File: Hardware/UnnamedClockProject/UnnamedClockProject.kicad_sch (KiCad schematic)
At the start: 28 parts, among them J101 CLOCK_OUT, J102 POWER, Q101 2N3904, U104 G3MB-202P, U105 G3MB-202P, U106 G3MB-202P, U107 CAT24C256

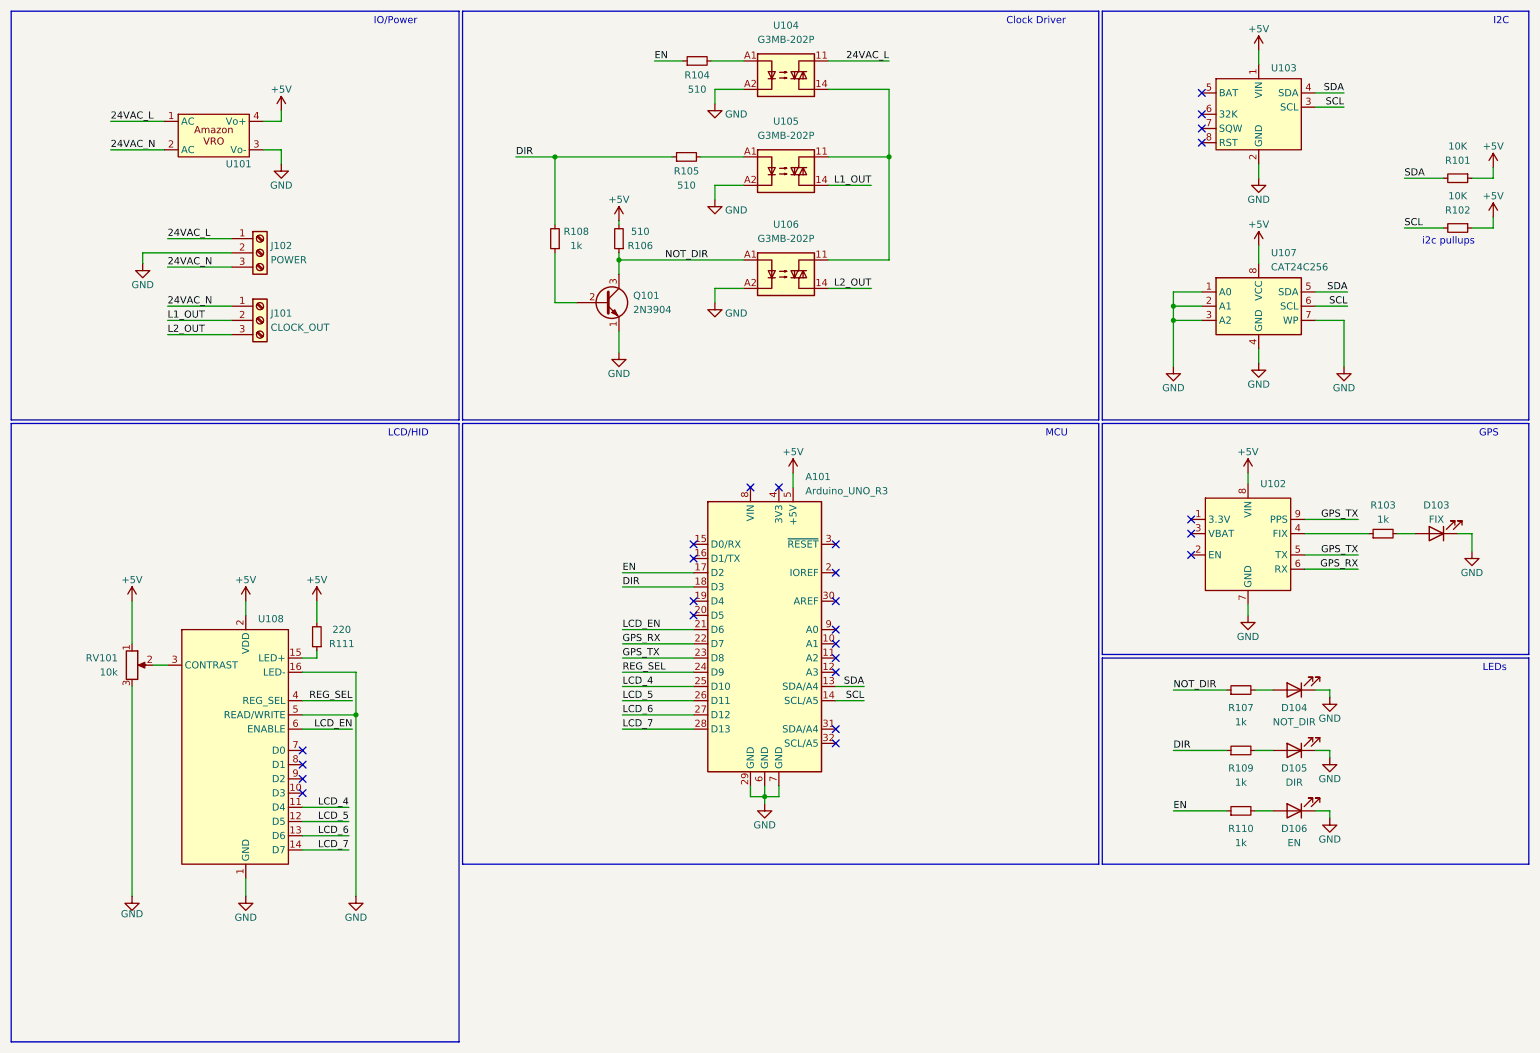
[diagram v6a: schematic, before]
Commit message: fix ERC
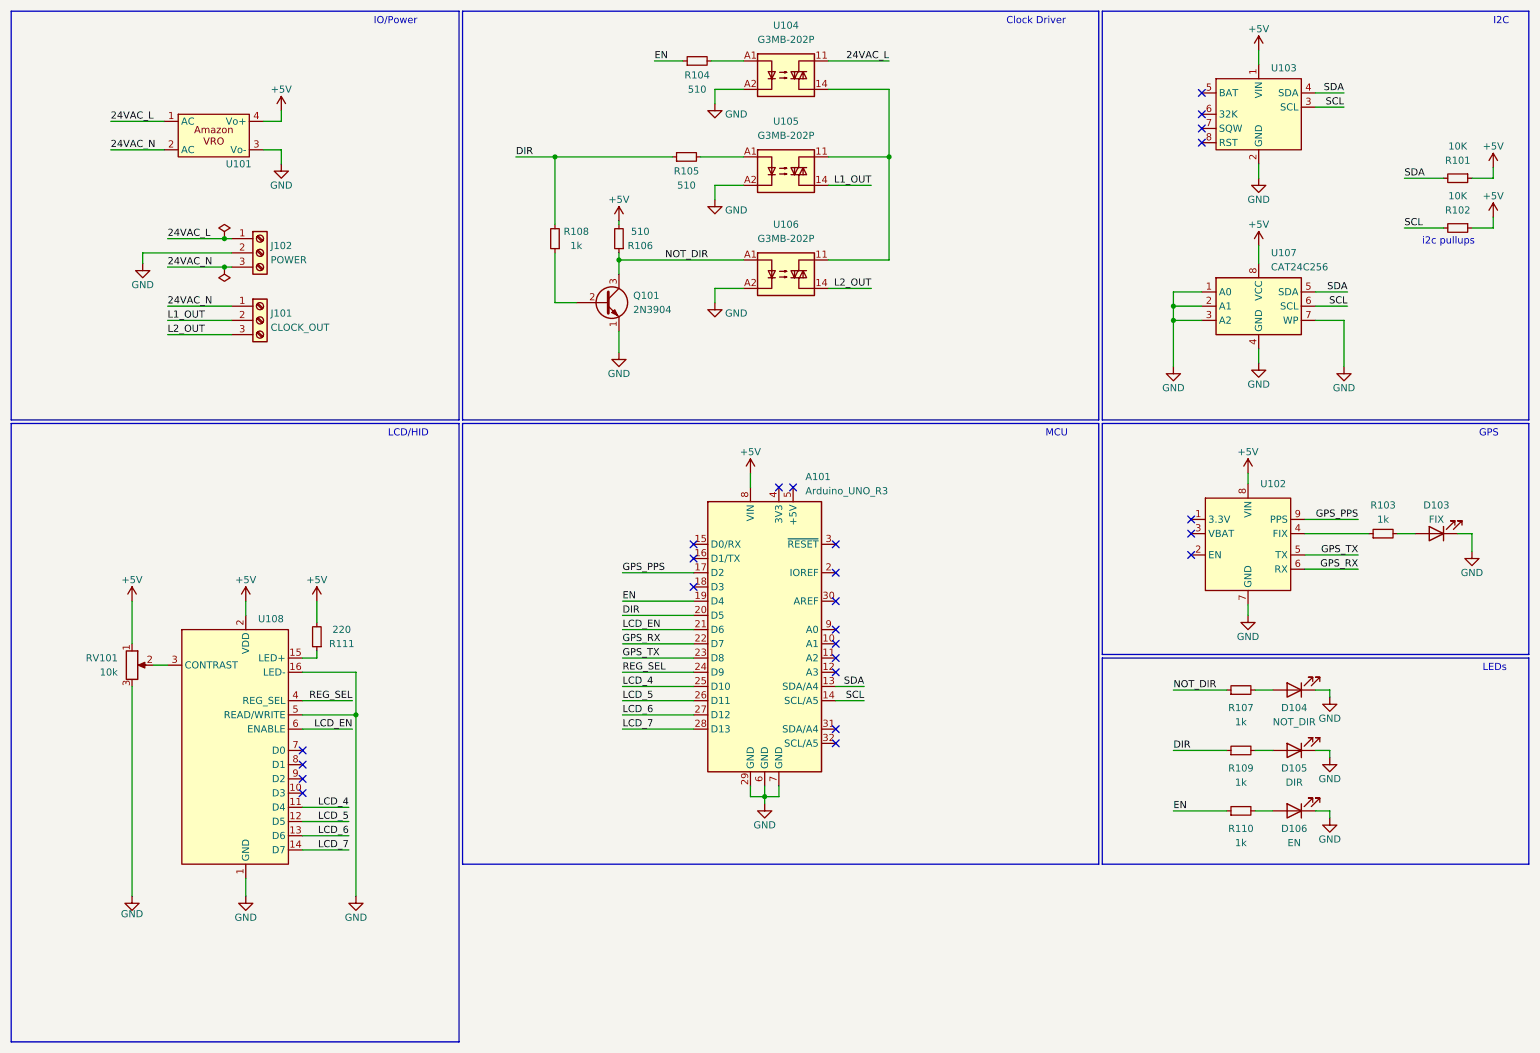
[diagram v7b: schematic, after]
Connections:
- net +5V: now also A101.8 (VIN); no longer A101.5 (+5V)
- net DIR: now also A101.20 (D5); no longer A101.18 (D3)
- net EN: now also A101.19 (D4); no longer A101.17 (D2)
- net GPS_TX: no longer U102.9 (PPS)
- new net GPS_PPS: A101.17 (D2), U102.9 (PPS)
- no-connect marks 26 -> 25

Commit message: bump
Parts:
- R101, R102, R103, R104, R105, R106, R107, R108, R109, R110, R111: footprint (none) -> Resistor_THT:R_Axial_DIN0207_L6.3mm_D2.5mm_P10.16mm_Horizontal
- RV101: footprint (none) -> Potentiometer_THT:Potentiometer_Bourns_3339S_Horizontal
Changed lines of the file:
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@@
       (effects (font (size 1.27 1.27)) (justify right))
     )
-    (property "Footprint" "" (at 34.925 129.54 0)
+    (property "Footprint" "Potentiometer_THT:Potentiometer_Bourns_3339S_Horizontal" (at 34.925 129.54 0)
       (effects (font (size 1.27 1.27)) hide)
     )
@@
       (effects (font (size 1.27 1.27)))
     )
-    (property "Footprint" "" (at 67.945 124.46 0)
+    (property "Footprint" "Resistor_THT:R_Axial_DIN0207_L6.3mm_D2.5mm_P10.16mm_Horizontal" (at 67.945 124.46 0)
       (effects (font (size 1.27 1.27)) hide)
     )
@@
       (effects (font (size 1.27 1.27)))
     )
-    (property "Footprint" "" (at 121.92 53.34 0)
+    (property "Footprint" "Resistor_THT:R_Axial_DIN0207_L6.3mm_D2.5mm_P10.16mm_Horizontal" (at 121.92 53.34 0)
       (effects (font (size 1.27 1.27)) hide)
     )
@@
       (effects (font (size 1.27 1.27)))
     )
-    (property "Footprint" "" (at 135.89 21.59 0)
+    (property "Footprint" "Resistor_THT:R_Axial_DIN0207_L6.3mm_D2.5mm_P10.16mm_Horizontal" (at 135.89 21.59 0)
       (effects (font (size 1.27 1.27)) hide)
     )
@@
       (effects (font (size 1.27 1.27)))
     )
-    (property "Footprint" "" (at 233.045 155.575 0)
+    (property "Footprint" "Resistor_THT:R_Axial_DIN0207_L6.3mm_D2.5mm_P10.16mm_Horizontal" (at 233.045 155.575 0)
       (effects (font (size 1.27 1.27)) hide)
     )
@@
       (effects (font (size 1.27 1.27)))
     )
-    (property "Footprint" "" (at 258.445 106.045 0)
+    (property "Footprint" "Resistor_THT:R_Axial_DIN0207_L6.3mm_D2.5mm_P10.16mm_Horizontal" (at 258.445 106.045 0)
       (effects (font (size 1.27 1.27)) hide)
     )
@@
       (effects (font (size 1.27 1.27)))
     )
-    (property "Footprint" "" (at 110.49 53.34 0)
+    (property "Footprint" "Resistor_THT:R_Axial_DIN0207_L6.3mm_D2.5mm_P10.16mm_Horizontal" (at 110.49 53.34 0)
       (effects (font (size 1.27 1.27)) hide)
     )
@@
       (effects (font (size 1.27 1.27)))
     )
-    (property "Footprint" "" (at 271.78 51.435 0)
+    (property "Footprint" "Resistor_THT:R_Axial_DIN0207_L6.3mm_D2.5mm_P10.16mm_Horizontal" (at 271.78 51.435 0)
       (effects (font (size 1.27 1.27)) hide)
     )
@@
       (effects (font (size 1.27 1.27)))
     )
-    (property "Footprint" "" (at 271.78 42.545 0)
+    (property "Footprint" "Resistor_THT:R_Axial_DIN0207_L6.3mm_D2.5mm_P10.16mm_Horizontal" (at 271.78 42.545 0)
       (effects (font (size 1.27 1.27)) hide)
     )
@@
       (effects (font (size 1.27 1.27)))
     )
-    (property "Footprint" "" (at 233.045 144.78 0)
+    (property "Footprint" "Resistor_THT:R_Axial_DIN0207_L6.3mm_D2.5mm_P10.16mm_Horizontal" (at 233.045 144.78 0)
       (effects (font (size 1.27 1.27)) hide)
     )
@@
       (effects (font (size 1.27 1.27)))
     )
-    (property "Footprint" "" (at 133.985 38.735 0)
+    (property "Footprint" "Resistor_THT:R_Axial_DIN0207_L6.3mm_D2.5mm_P10.16mm_Horizontal" (at 133.985 38.735 0)
       (effects (font (size 1.27 1.27)) hide)
     )
@@
       (effects (font (size 1.27 1.27)))
     )
-    (property "Footprint" "" (at 233.045 133.985 0)
-      (effects (font (size 1.27 1.27)) hide)
-    )
+    (property "Footprint" "Resistor_THT:R_Axial_DIN0207_L6.3mm_D2.5mm_P10.16mm_Horizontal" (at 233.045 133.985 0)
+      (effects (font (size 1.27 1.27)) hide)
+    )
